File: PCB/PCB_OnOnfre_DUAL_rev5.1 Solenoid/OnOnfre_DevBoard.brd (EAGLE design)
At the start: 44 x 41.7 mm, 28 parts, among them J1 9PIN 2.54MM, J3Y S8050, J7 8p, K1 PA1A-6VV, K2 PA1A-6VV, U2 esp12

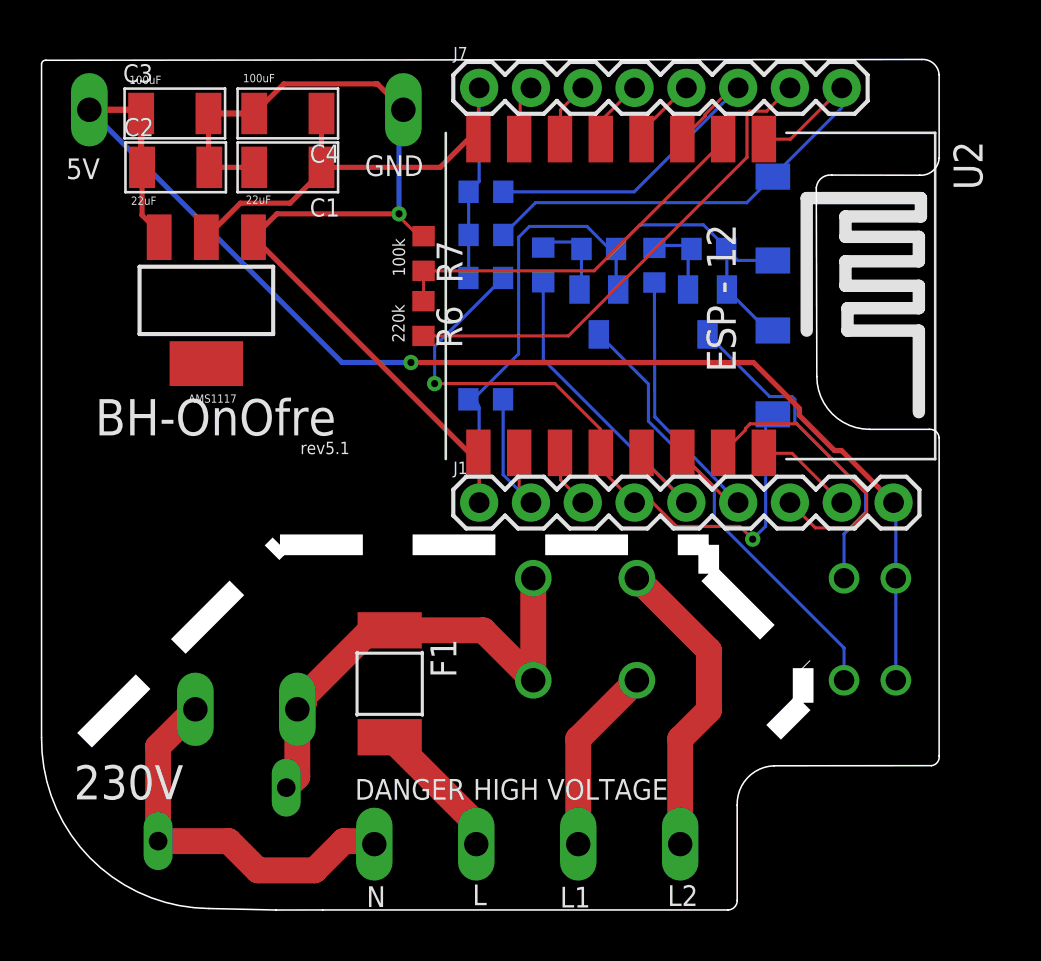
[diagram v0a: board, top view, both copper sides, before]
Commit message: Revert "sol"
This reverts commit 5e2c5b42127c6a8382e434407ba92e7f1eb271ca.
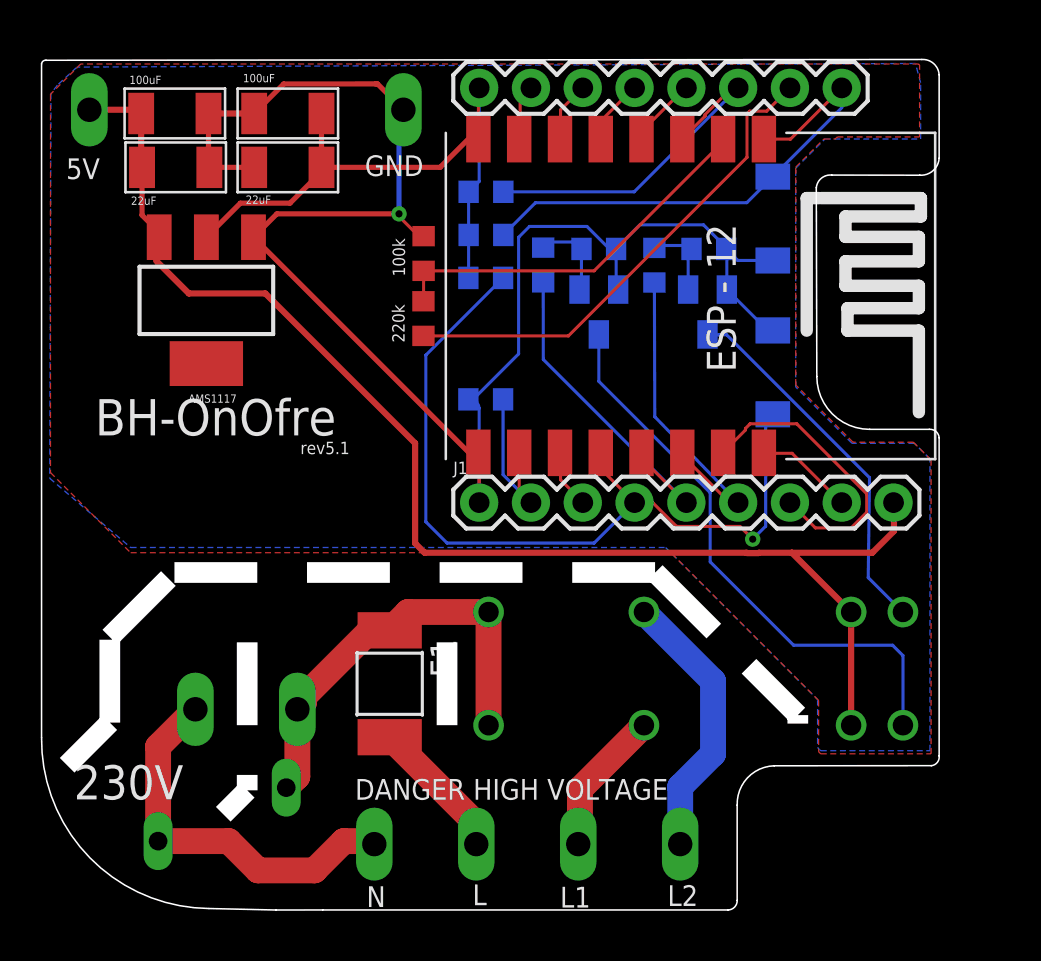
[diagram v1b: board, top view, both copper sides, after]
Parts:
- K1, K2: value PA1A-6VV -> OMRON-G3MB-202P-SSR2; device relay:PA -> Omron G3MB 202p SSR:OMRON-G3MB-202P-SSR
- moved K1 6.11 mm to (35.3, 13.7), turned to 180 degrees
- moved K2 4.94 mm to (35.3, 19.3), turned to 180 degrees
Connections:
- net LINE_L: now also K1.1, K2.1; no longer K1.COM, K2.COM
- net LINE_ONE_OUT: now also K1.2; no longer K2.NO
- net LINE_TWO_OUT: now also K2.2; no longer K1.NO
- net N$1: now also K1.4; no longer K2.2
- net N$9: now also K2.4; no longer K1.2
- net VCC: now also K1.3, K2.3; no longer K1.1, K2.1
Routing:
- net GPIO0: track 33.6 -> 41.4 mm, vias 2 -> 1
- net N$1: track 21.9 -> 28.2 mm
- net LINE_L: track 23.4 -> 21.1 mm
- net LINE_ONE_OUT: track 9.23 -> 7.16 mm
- net N$9: track 16.3 -> 18.2 mm
- net LINE_TWO_OUT: track 15.1 -> 13.5 mm
- net VCC: track 66.0 -> 67.4 mm, vias 1 -> 0
- added copper zone on layer 1, net GND
- added copper zone on layer 16, net GND
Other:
- outline, holes or cut-outs redrawn
